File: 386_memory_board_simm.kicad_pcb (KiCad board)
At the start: 4 copper layers, 222.2 x 85.7 mm, 76 parts, among them J1 Bus_386_Memory, U10 74LS174, U11 74LS174, U12 74LS174, U13 74LS174, U14 74LS158, U15 74LS158, U16 74LS158, U17 74F10, U18 SPARE, U19 SPARE, U37 74F10, U38 74F00, U39 74F00, U40 74F10, U43 74F02, U44 74F10, U45 74LS04, U5 74LS174, U6 74LS174, U7 74LS158, U8 74LS158, U9 74LS158

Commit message: final touchups before ordering first boards
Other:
- board text added: "Intel 301 Memory Board Replica"
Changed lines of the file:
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@@
 		(layer "Edge.Cuts")
+	)
+	(gr_text "Intel 301 Memory Board Replica"
+		(at 259.715 144.78 0)
+		(layer "F.SilkS")
+		(effects
+			(font
+				(size 2 2)
+				(thickness 0.3)
+			)
+			(justify left bottom)
+		)
 	)
 	(gr_text "BANK0\n"

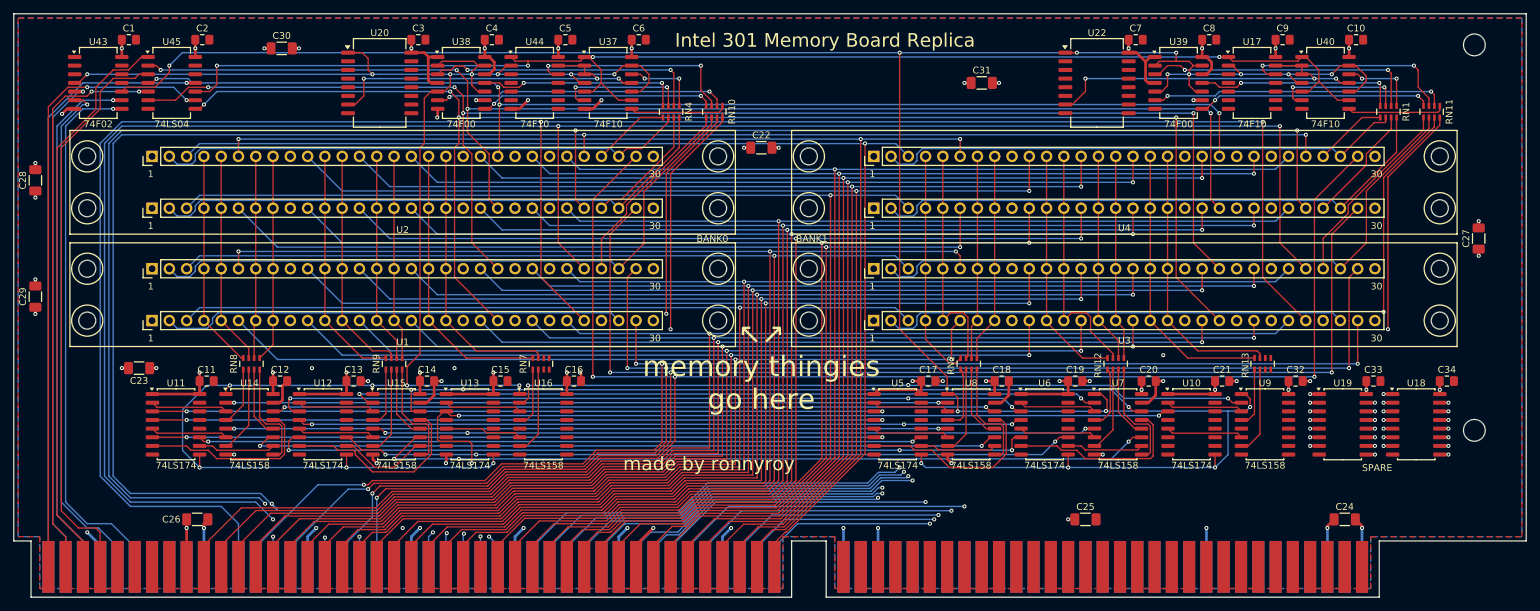
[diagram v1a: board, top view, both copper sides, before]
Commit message: PCB Revision 2 -implements 8MB operation -fixed the missing slot cutout on rev.1 -overhauls the slot connector based on i440bx's discoveries and design -add information to modify rev.1 Boards to 8MB
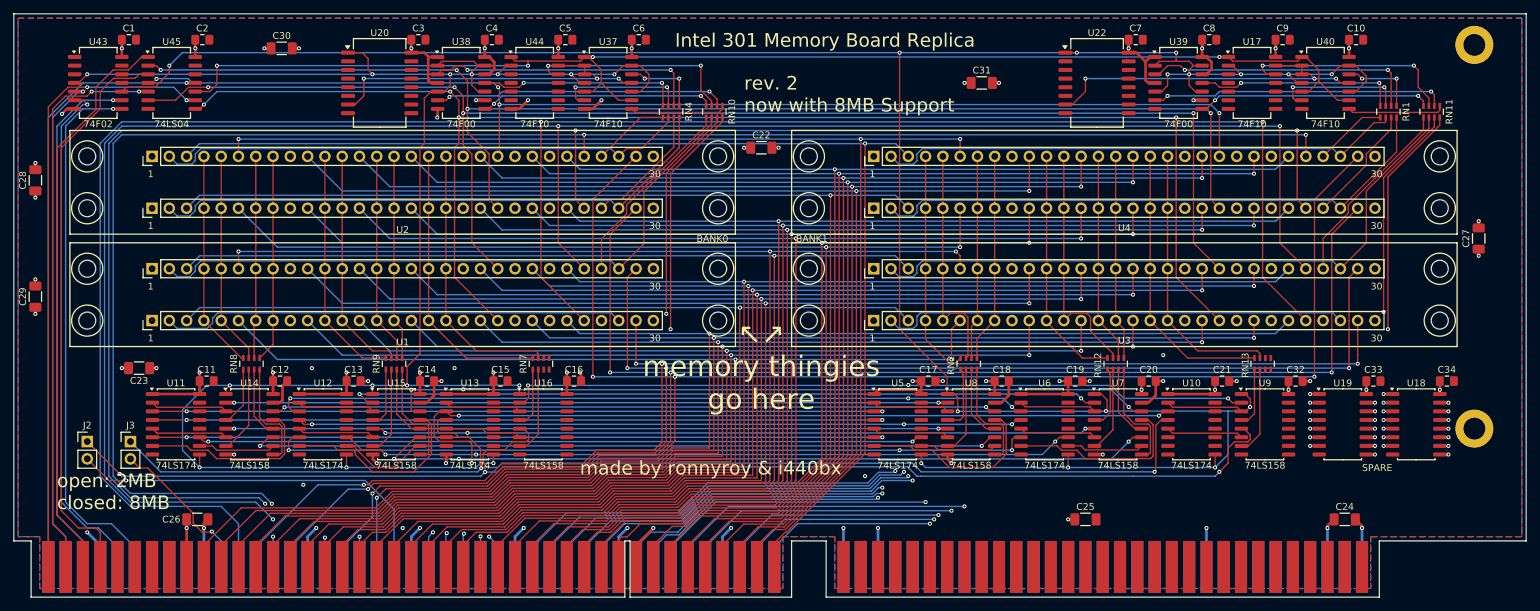
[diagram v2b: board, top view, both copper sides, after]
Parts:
- removed REF** (x2): MountingHole_3.2mm_M3_DIN965, MountingHole:MountingHole_3.2mm_M3_DIN965
- added H1: MountingHole, MountingHole:MountingHole_3.2mm_M3_DIN965_Pad, F.Cu at (377.2, 144.3)
- added H2: MountingHole, MountingHole:MountingHole_3.2mm_M3_DIN965_Pad, F.Cu at (377.2, 200.7)
- added J2: Conn_01x02_Pin, Connector_PinHeader_2.54mm:PinHeader_1x02_P2.54mm_Vertical, F.Cu at (173.4, 202.6)
- added J3: Conn_01x02_Pin, Connector_PinHeader_2.54mm:PinHeader_1x02_P2.54mm_Vertical, F.Cu at (179.7, 202.6)
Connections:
- net PIN100 renamed SLEB0
- net PIN101 renamed SLEB1
- net PIN103 renamed RMSEL0
- net PIN104 renamed RMSEL1
- net PIN105 renamed MEMREF
- net ~{PIN105} renamed ~{MEMREF}
- J1 pad 85: unconnected-(J1-NC-Pad85) -> CPUA21
- J1 pad 95: unconnected-(J1-NC-Pad95) -> CPUA22
- U10 pad 4: unconnected-(U10-D1-Pad4) -> A9B
- U13 pad 4: unconnected-(U13-D1-Pad4) -> A9B
- U16 pad 5: unconnected-(U16-I0b-Pad5) -> A9A
- U9 pad 5: unconnected-(U9-I0b-Pad5) -> A9A
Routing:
- net A9A: track 0.00 -> 192.9 mm, vias 0 -> 3
- net A9B: track 0.00 -> 175.4 mm, vias 0 -> 2
- net CPUA21: track 0.00 -> 56.6 mm, vias 0 -> 1
- net CPUA22: track 0.00 -> 23.0 mm, vias 0 -> 1
- net DOUT8R3: track 277.8 -> 275.4 mm
- net A8B: track 135.4 -> 136.2 mm
- net VCC: vias 40 -> 42
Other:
- outline, holes or cut-outs redrawn
- board text added: "Front: VSS In1: VSS IN2: VCC Back: VCC"
- board text added: "^ cutout"
- board text added: "made by ronnyroy & i440bx"
- board text added: "open: 2MB closed: 8MB"
- board text added: "rev. 2 now with 8MB Support"
- board text removed: "Front: Horizontal VSS In1: VSS IN2: VCC Back: Vertical VCC"
- board text removed: "made by ronnyroy"
